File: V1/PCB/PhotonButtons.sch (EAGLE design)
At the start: 25 parts, among them Q1 MOSFET-NCHANNEL2N7002PW

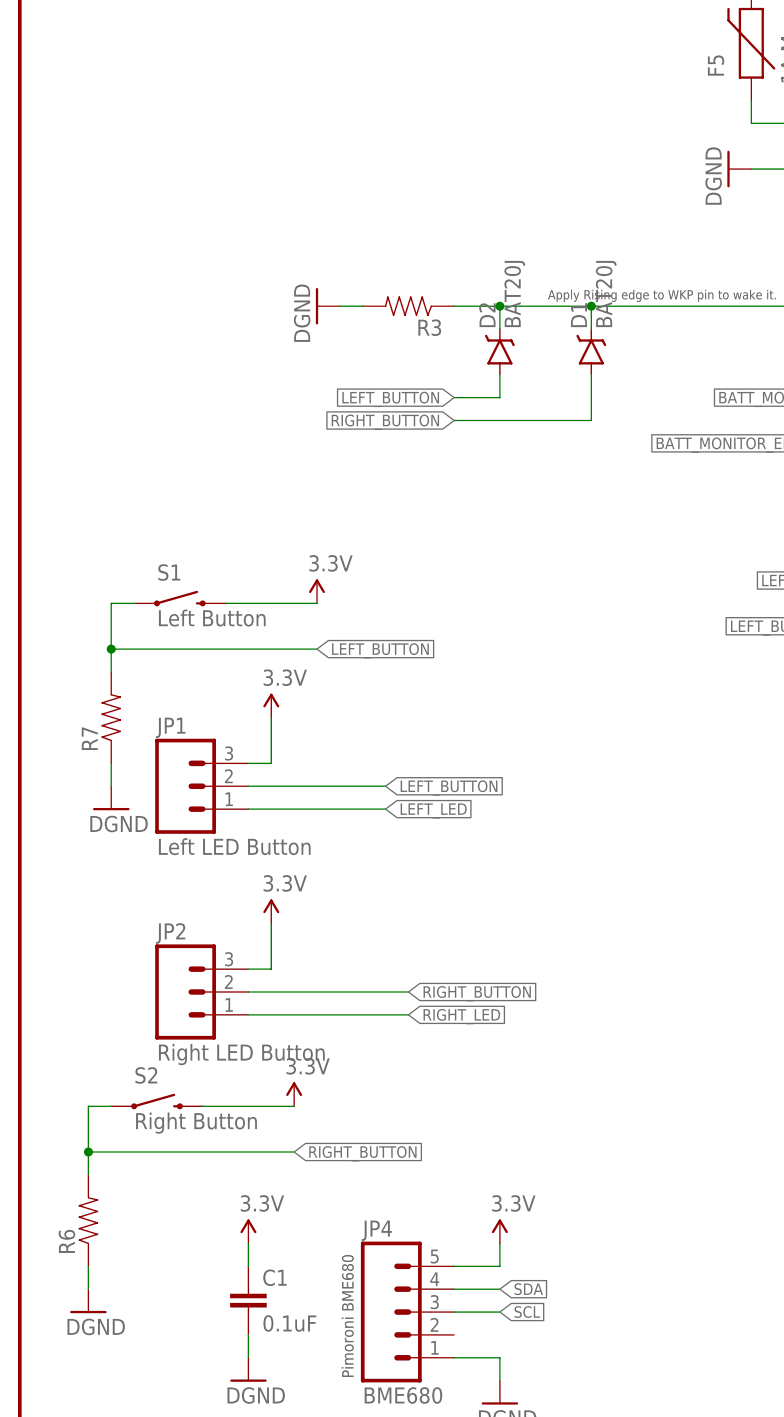
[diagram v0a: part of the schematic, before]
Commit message: Added components values
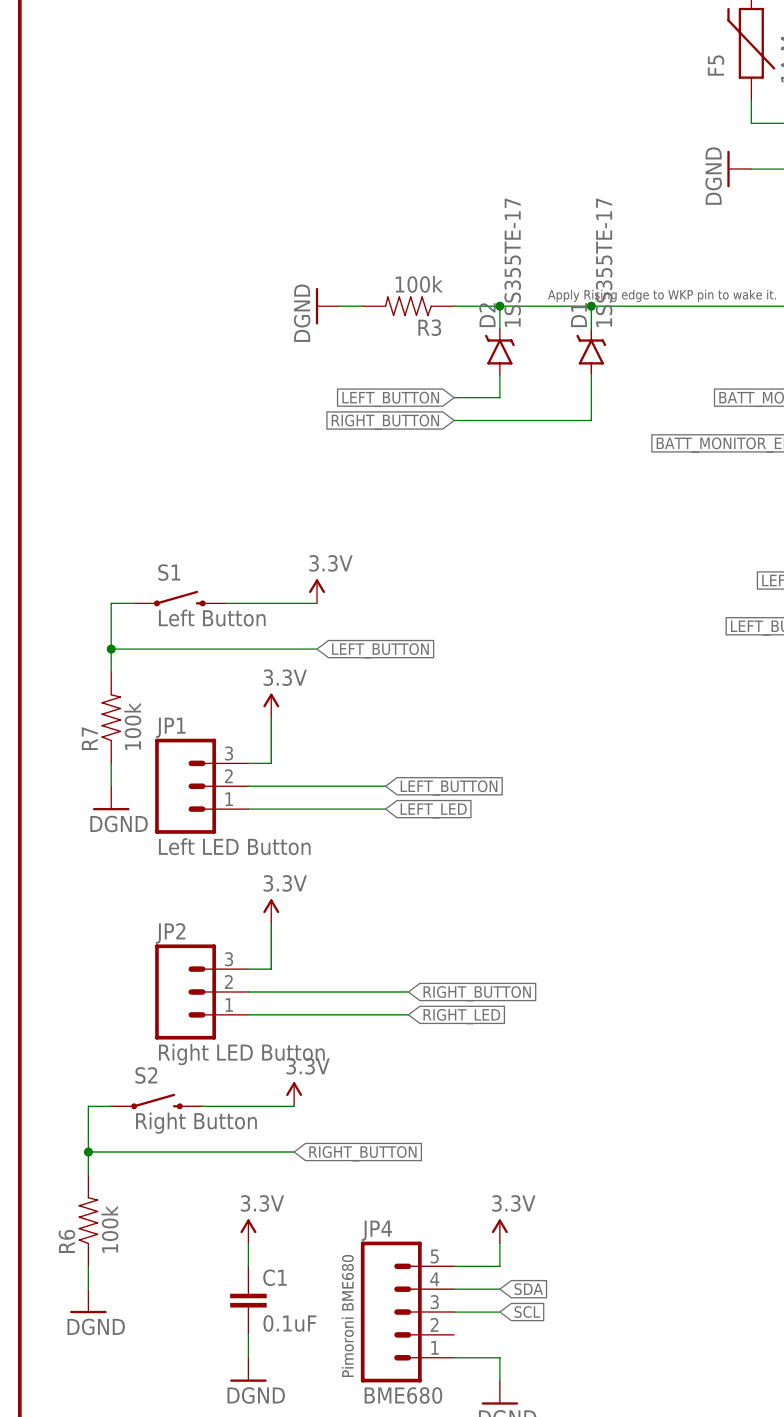
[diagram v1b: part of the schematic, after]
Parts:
- D1, D2: value BAT20J -> 1SS355TE-17; FARNELL (none) -> 152-5435
- Q1: FARNELL (none) -> 189-4713
- R3, R6, R7: value (none) -> 100k
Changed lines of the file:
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@@
 <part name="U$1" library="Tinamous" deviceset="PHOTON_SMD" device=""/>
 <part name="R5" library="SparkFun-Resistors" deviceset="RESISTOR" device="0805-RES" value="100k"/>
-<part name="R6" library="SparkFun-Resistors" deviceset="RESISTOR" device="0805-RES"/>
-<part name="R7" library="SparkFun-Resistors" deviceset="RESISTOR" device="0805-RES"/>
+<part name="R6" library="SparkFun-Resistors" deviceset="RESISTOR" device="0805-RES" value="100k"/>
+<part name="R7" library="SparkFun-Resistors" deviceset="RESISTOR" device="0805-RES" value="100k"/>
 <part name="JP1" library="SparkFun-Connectors" deviceset="M03" device="POLAR" value="Left LED Button"/>
 <part name="JP2" library="SparkFun-Connectors" deviceset="M03" device="POLAR" value="Right LED Button"/>
@@
 <part name="LOGO1" library="SparkFun-Aesthetics" deviceset="OSHW-LOGO" device="L"/>
 <part name="JP3" library="SparkFun-Connectors" deviceset="M02" device="-JST-2MM-SMT"/>
-<part name="D1" library="SparkFun-DiscreteSemi" deviceset="DIODE-SCHOTTKY" device="-BAT20J" value="BAT20J"/>
-<part name="D2" library="SparkFun-DiscreteSemi" deviceset="DIODE-SCHOTTKY" device="-BAT20J" value="BAT20J"/>
+<part name="D1" library="SparkFun-DiscreteSemi" deviceset="DIODE-SCHOTTKY" device="-BAT20J" value="1SS355TE-17">
+<attribute name="FARNELL" value="152-5435"/>
+</part>
+<part name="D2" library="SparkFun-DiscreteSemi" deviceset="DIODE-SCHOTTKY" device="-BAT20J" value="1SS355TE-17">
+<attribute name="FARNELL" value="152-5435"/>
+</part>
 <part name="GND2" library="SparkFun-Aesthetics" deviceset="DGND" device=""/>
 <part name="GND3" library="SparkFun-Aesthetics" deviceset="DGND" device=""/>
@@
 <part name="SUPPLY12" library="SparkFun-Aesthetics" deviceset="3.3V" device=""/>
 <part name="GND10" library="SparkFun-Aesthetics" deviceset="DGND" device=""/>
-<part name="Q1" library="SparkFun-DiscreteSemi" deviceset="MOSFET-NCHANNEL" device="2N7002PW"/>
+<part name="Q1" library="SparkFun-DiscreteSemi" deviceset="MOSFET-NCHANNEL" device="2N7002PW">
+<attribute name="FARNELL" value="189-4713"/>
+</part>
 <part name="GND4" library="SparkFun-Aesthetics" deviceset="DGND" device=""/>
 <part name="R2" library="SparkFun-Resistors" deviceset="RESISTOR" device="0805-RES" value="1M"/>
@@
 <part name="LOGO2" library="SparkFun-Aesthetics" deviceset="OSHW-LOGO" device="L"/>
 <part name="H3" library="holes" deviceset="MOUNT-HOLE" device="3.2"/>
-<part name="R3" library="SparkFun-Resistors" deviceset="RESISTOR" device="0805-RES"/>
+<part name="R3" library="SparkFun-Resistors" deviceset="RESISTOR" device="0805-RES" value="100k"/>
 <part name="GND7" library="SparkFun-Aesthetics" deviceset="DGND" device=""/>
 </parts>
@@
 <instance part="LOGO1" gate="G$1" x="132.08" y="10.16"/>
 <instance part="JP3" gate="G$1" x="218.44" y="63.5" rot="R180"/>
-<instance part="D1" gate="G$1" x="63.5" y="127" rot="R90"/>
-<instance part="D2" gate="G$1" x="53.34" y="127" rot="R90"/>
+<instance part="D1" gate="G$1" x="63.5" y="127" rot="R90">
+<attribute name="FARNELL" x="63.5" y="127" size="1.778" layer="96" rot="R90" display="off"/>
+</instance>
+<instance part="D2" gate="G$1" x="53.34" y="127" rot="R90">
+<attribute name="FARNELL" x="53.34" y="127" size="1.778" layer="96" rot="R90" display="off"/>
+</instance>
 <instance part="GND2" gate="G$1" x="10.16" y="76.2"/>
 <instance part="GND3" gate="G$1" x="7.62" y="20.32"/>
@@
 <instance part="SUPPLY12" gate="G$1" x="25.4" y="27.94"/>
 <instance part="GND10" gate="G$1" x="25.4" y="12.7"/>
-<instance part="Q1" gate="G$1" x="180.34" y="53.34"/>
+<instance part="Q1" gate="G$1" x="180.34" y="53.34">
+<attribute name="FARNELL" x="180.34" y="53.34" size="1.778" layer="96" display="off"/>
+</instance>
 <instance part="GND4" gate="G$1" x="180.34" y="43.18"/>
 <instance part="R2" gate="G$1" x="165.1" y="45.72" rot="R90"/>
